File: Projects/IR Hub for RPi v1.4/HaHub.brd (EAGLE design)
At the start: 65 x 56 mm, 39 parts, among them SW1 SPST_TACT-KMR2, SW2 SPST_TACT-KMR2, SW3 SPST_TACT-KMR2, T1 2N4401, T2 2N4401, T3 2N4401, T4 2N4401

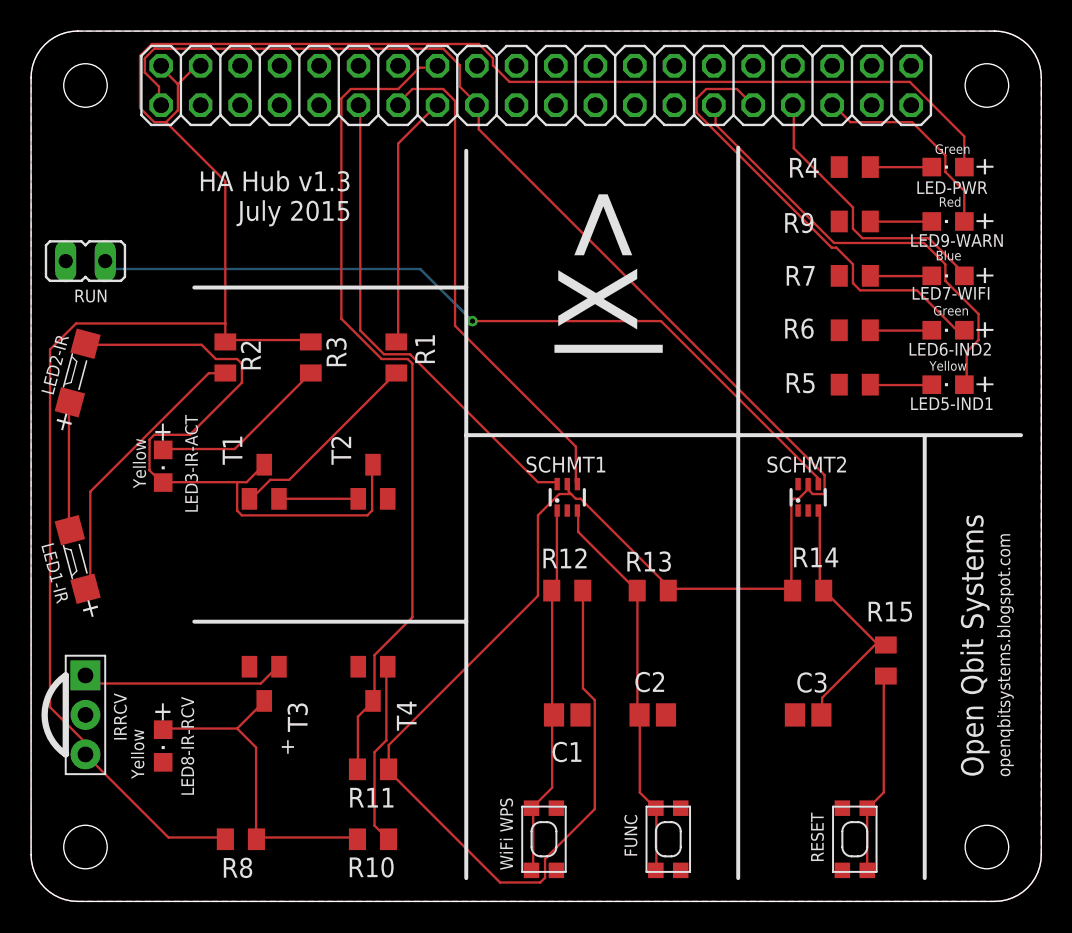
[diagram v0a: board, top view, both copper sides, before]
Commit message: Copied the v1.3 into v1.4 folder, and noted down v1.3 LED and buttons locations
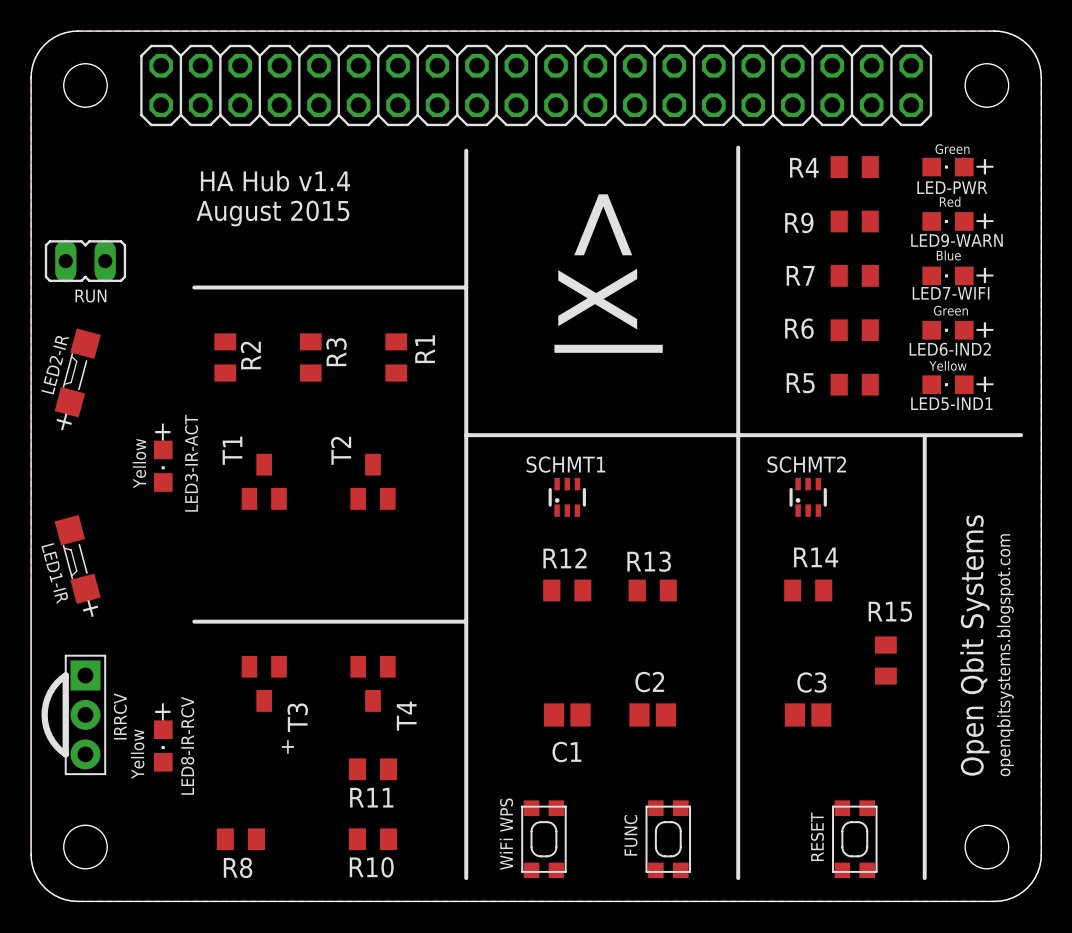
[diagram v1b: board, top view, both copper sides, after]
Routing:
- net +3V3: track 144.9 -> 0.00 mm
- net +5V: track 141.5 -> 0.00 mm
- net GPIO23: track 54.6 -> 0.00 mm
- net RST: track 52.0 -> 0.00 mm, vias 1 -> 0
- net N$4: track 43.2 -> 0.00 mm
- net GPIO27: track 32.4 -> 0.00 mm
- net GPIO17: track 31.4 -> 0.00 mm
- net GPIO06: track 29.1 -> 0.00 mm
- net GPIO05: track 28.9 -> 0.00 mm
- net N$12: track 25.3 -> 0.00 mm
- net N$9: track 24.1 -> 0.00 mm
- net N$10: track 21.5 -> 0.00 mm
- net N$2: track 18.2 -> 0.00 mm
- net GPIO13: track 18.1 -> 0.00 mm
- net N$13: track 17.5 -> 0.00 mm
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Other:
- board text added: "HA Hub v1.4 August 2015"
- board text added: "Home Automation Hub v1.4"
- board text removed: "HA Hub v1.3 July 2015"
- board text removed: "Home Automation Hub v1.3"
- board text removed: "TODO DONE 1. Check the Schmitt debouncing on breadboard 2. Check both ICs wrt 74HC/74LV/... for 3.3V1. check the polarity of the IR LEDs 3. Add schmitt buffers for all the push buttons (create part) 4. ELIMINATED - Verify the Watchdog circuit 5. ELIMINATED - Will RPi gpio go in a state to allow disabling WD? 6. Ensure long push for RESET push button (cap and resistor values) 7. Move Power LED to 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"
